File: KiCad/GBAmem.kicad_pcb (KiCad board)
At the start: 4 copper layers, 18.2 x 18.3 mm, 2 parts, among them IC1 IS62WV12816EBLL-45TLI, U1 HY62LF16206A-LT12C

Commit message: Add build files and initial code
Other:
- board text added: "github.com/HorstBaerbel/GBA-mem v1.0"
- board text removed: "github.com/HorstBaerbel/GBAmem v1.0"
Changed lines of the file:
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@@
       (effects (font (size 1.27 1.27) (thickness 0.254)))
     )
+    (fp_line (start -6.625 -9.52) (end 6.625 -9.52) (layer F.CrtYd) (width 0.05))
+    (fp_line (start 6.625 -9.52) (end 6.625 9.52) (layer F.CrtYd) (width 0.05))
+    (fp_line (start 6.625 9.52) (end -6.625 9.52) (layer F.CrtYd) (width 0.05))
+    (fp_line (start -6.625 9.52) (end -6.625 -9.52) (layer F.CrtYd) (width 0.05))
+    (fp_line (start -5.08 -9.205) (end 5.08 -9.205) (layer F.Fab) (width 0.1))
+    (fp_line (start 5.08 -9.205) (end 5.08 9.205) (layer F.Fab) (width 0.1))
+    (fp_line (start 5.08 9.205) (end -5.08 9.205) (layer F.Fab) (width 0.1))
+    (fp_line (start -5.08 9.205) (end -5.08 -9.205) (layer F.Fab) (width 0.1))
+    (fp_line (start -5.08 -8.405) (end -4.28 -9.205) (layer F.Fab) (width 0.1))
+    (fp_line (start -4.73 -9.205) (end 4.73 -9.205) (layer F.SilkS) (width 0.2))
+    (fp_line (start 4.73 -9.205) (end 4.73 9.205) (layer F.SilkS) (width 0.2))
+    (fp_line (start 4.73 9.205) (end -4.73 9.205) (layer F.SilkS) (width 0.2))
+    (fp_line (start -4.73 9.205) (end -4.73 -9.205) (layer F.SilkS) (width 0.2))
     (fp_line (start -6.375 -9.05) (end -5.08 -9.05) (layer F.SilkS) (width 0.2))
-    (fp_line (start -4.73 9.205) (end -4.73 -9.205) (layer F.SilkS) (width 0.2))
-    (fp_line (start 4.73 9.205) (end -4.73 9.205) (layer F.SilkS) (width 0.2))
-    (fp_line (start 4.73 -9.205) (end 4.73 9.205) (layer F.SilkS) (width 0.2))
-    (fp_line (start -4.73 -9.205) (end 4.73 -9.205) (layer F.SilkS) (width 0.2))
-    (fp_line (start -5.08 -8.405) (end -4.28 -9.205) (layer F.Fab) (width 0.1))
-    (fp_line (start -5.08 9.205) (end -5.08 -9.205) (layer F.Fab) (width 0.1))
-    (fp_line (start 5.08 9.205) (end -5.08 9.205) (layer F.Fab) (width 0.1))
-    (fp_line (start 5.08 -9.205) (end 5.08 9.205) (layer F.Fab) (width 0.1))
-    (fp_line (start -5.08 -9.205) (end 5.08 -9.205) (layer F.Fab) (width 0.1))
-    (fp_line (start -6.625 9.52) (end -6.625 -9.52) (layer F.CrtYd) (width 0.05))
-    (fp_line (start 6.625 9.52) (end -6.625 9.52) (layer F.CrtYd) (width 0.05))
-    (fp_line (start 6.625 -9.52) (end 6.625 9.52) (layer F.CrtYd) (width 0.05))
-    (fp_line (start -6.625 -9.52) (end 6.625 -9.52) (layer F.CrtYd) (width 0.05))
     (fp_text user %R (at 0 0) (layer F.Fab) hide
       (effects (font (size 1.27 1.27) (thickness 0.254)))
@@
       (effects (font (size 0.8 0.8) (thickness 0.125)) (justify mirror))
     )
+    (fp_line (start 9.6 6.3) (end 9.6 -6.3) (layer B.CrtYd) (width 0.12))
+    (fp_line (start 9.6 -6.3) (end -9.2 -6.3) (layer B.CrtYd) (width 0.12))
+    (fp_line (start -9.2 -6.3) (end -9.2 6.3) (layer B.CrtYd) (width 0.12))
+    (fp_line (start -9.2 6.3) (end 9.6 6.3) (layer B.CrtYd) (width 0.12))
+    (fp_line (start 8.4 -6.1) (end 8.4 6.1) (layer B.Fab) (width 0.12))
+    (fp_line (start 8.4 6.1) (end -8 6.1) (layer B.Fab) (width 0.12))
+    (fp_line (start -8 6.1) (end -8 -6.1) (layer B.Fab) (width 0.12))
     (fp_line (start -8 -6.1) (end 8.4 -6.1) (layer B.Fab) (width 0.12))
-    (fp_line (start -8 6.1) (end -8 -6.1) (layer B.Fab) (width 0.12))
-    (fp_line (start 8.4 6.1) (end -8 6.1) (layer B.Fab) (width 0.12))
-    (fp_line (start 8.4 -6.1) (end 8.4 6.1) (layer B.Fab) (width 0.12))
-    (fp_line (start -9.2 6.3) (end 9.6 6.3) (layer B.CrtYd) (width 0.12))
-    (fp_line (start -9.2 -6.3) (end -9.2 6.3) (layer B.CrtYd) (width 0.12))
-    (fp_line (start 9.6 -6.3) (end -9.2 -6.3) (layer B.CrtYd) (width 0.12))
-    (fp_line (start 9.6 6.3) (end 9.6 -6.3) (layer B.CrtYd) (width 0.12))
     (fp_text user "Flipped / Breakout" (at 0 5.3) (layer B.CrtYd)
       (effects (font (size 0.7 0.7) (thickness 0.125)) (justify mirror))
@@
     (effects (font (size 0.8 0.8) (thickness 0.2)))
   )
-  (gr_text "github.com/HorstBaerbel/GBAmem v1.0" (at 171.0055 89.789 90) (layer F.SilkS)
-    (effects (font (size 0.58 0.58) (thickness 0.125)))
+  (gr_text "github.com/HorstBaerbel/GBA-mem v1.0" (at 171.0055 89.789 90) (layer F.SilkS)
+    (effects (font (size 0.56 0.56) (thickness 0.125)))
   )
   (segment (start 169.3758 93.293) (end 169.3758 92.36) (width 0.1) (layer Front) (net 1))

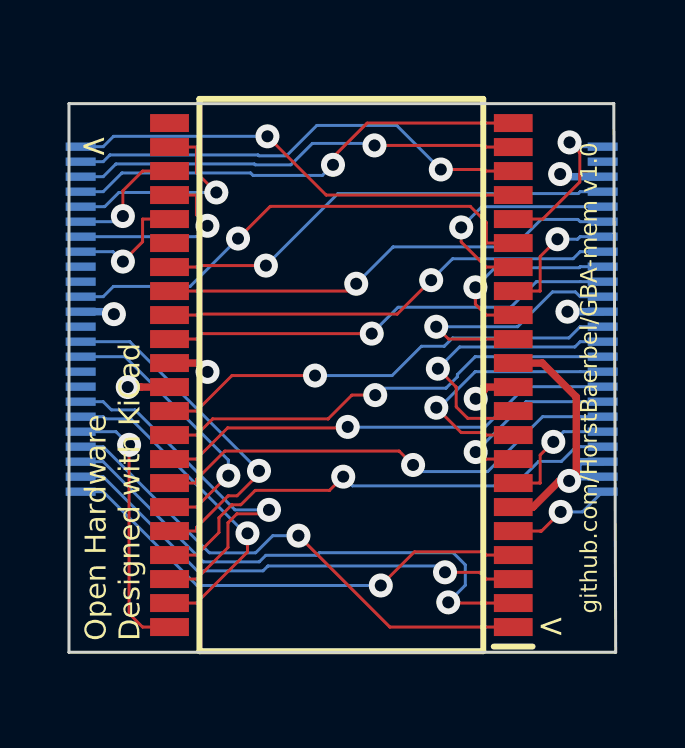
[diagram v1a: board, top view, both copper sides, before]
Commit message: Update PCB with positioning markers
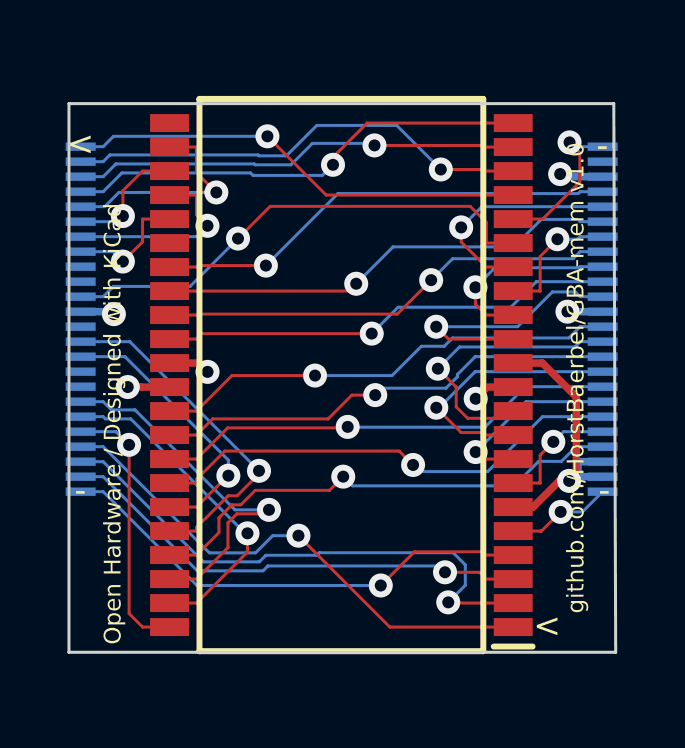
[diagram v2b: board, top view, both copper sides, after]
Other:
- board text added: "-"
- board text added: "Open Hardware / Designed with KiCad"
- board text removed: "Open Hardware Designed with KiCad"
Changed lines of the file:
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@@
   (general
     (thickness 1.6)
-    (drawings 8)
+    (drawings 11)
     (tracks 365)
     (zones 0)
@@
       (effects (font (size 1.27 1.27) (thickness 0.254)))
     )
+    (fp_line (start -6.375 -9.05) (end -5.08 -9.05) (layer F.SilkS) (width 0.2))
+    (fp_line (start -4.73 9.205) (end -4.73 -9.205) (layer F.SilkS) (width 0.2))
+    (fp_line (start 4.73 9.205) (end -4.73 9.205) (layer F.SilkS) (width 0.2))
+    (fp_line (start 4.73 -9.205) (end 4.73 9.205) (layer F.SilkS) (width 0.2))
+    (fp_line (start -4.73 -9.205) (end 4.73 -9.205) (layer F.SilkS) (width 0.2))
+    (fp_line (start -5.08 -8.405) (end -4.28 -9.205) (layer F.Fab) (width 0.1))
+    (fp_line (start -5.08 9.205) (end -5.08 -9.205) (layer F.Fab) (width 0.1))
+    (fp_line (start 5.08 9.205) (end -5.08 9.205) (layer F.Fab) (width 0.1))
+    (fp_line (start 5.08 -9.205) (end 5.08 9.205) (layer F.Fab) (width 0.1))
+    (fp_line (start -5.08 -9.205) (end 5.08 -9.205) (layer F.Fab) (width 0.1))
+    (fp_line (start -6.625 9.52) (end -6.625 -9.52) (layer F.CrtYd) (width 0.05))
+    (fp_line (start 6.625 9.52) (end -6.625 9.52) (layer F.CrtYd) (width 0.05))
+    (fp_line (start 6.625 -9.52) (end 6.625 9.52) (layer F.CrtYd) (width 0.05))
     (fp_line (start -6.625 -9.52) (end 6.625 -9.52) (layer F.CrtYd) (width 0.05))
-    (fp_line (start 6.625 -9.52) (end 6.625 9.52) (layer F.CrtYd) (width 0.05))
-    (fp_line (start 6.625 9.52) (end -6.625 9.52) (layer F.CrtYd) (width 0.05))
-    (fp_line (start -6.625 9.52) (end -6.625 -9.52) (layer F.CrtYd) (width 0.05))
-    (fp_line (start -5.08 -9.205) (end 5.08 -9.205) (layer F.Fab) (width 0.1))
-    (fp_line (start 5.08 -9.205) (end 5.08 9.205) (layer F.Fab) (width 0.1))
-    (fp_line (start 5.08 9.205) (end -5.08 9.205) (layer F.Fab) (width 0.1))
-    (fp_line (start -5.08 9.205) (end -5.08 -9.205) (layer F.Fab) (width 0.1))
-    (fp_line (start -5.08 -8.405) (end -4.28 -9.205) (layer F.Fab) (width 0.1))
-    (fp_line (start -4.73 -9.205) (end 4.73 -9.205) (layer F.SilkS) (width 0.2))
-    (fp_line (start 4.73 -9.205) (end 4.73 9.205) (layer F.SilkS) (width 0.2))
-    (fp_line (start 4.73 9.205) (end -4.73 9.205) (layer F.SilkS) (width 0.2))
-    (fp_line (start -4.73 9.205) (end -4.73 -9.205) (layer F.SilkS) (width 0.2))
-    (fp_line (start -6.375 -9.05) (end -5.08 -9.05) (layer F.SilkS) (width 0.2))
     (fp_text user %R (at 0 0) (layer F.Fab) hide
       (effects (font (size 1.27 1.27) (thickness 0.254)))
@@
       (effects (font (size 0.8 0.8) (thickness 0.125)) (justify mirror))
     )
+    (fp_line (start -8 -6.1) (end 8.4 -6.1) (layer B.Fab) (width 0.12))
+    (fp_line (start -8 6.1) (end -8 -6.1) (layer B.Fab) (width 0.12))
+    (fp_line (start 8.4 6.1) (end -8 6.1) (layer B.Fab) (width 0.12))
+    (fp_line (start 8.4 -6.1) (end 8.4 6.1) (layer B.Fab) (width 0.12))
+    (fp_line (start -9.2 6.3) (end 9.6 6.3) (layer B.CrtYd) (width 0.12))
+    (fp_line (start -9.2 -6.3) (end -9.2 6.3) (layer B.CrtYd) (width 0.12))
+    (fp_line (start 9.6 -6.3) (end -9.2 -6.3) (layer B.CrtYd) (width 0.12))
     (fp_line (start 9.6 6.3) (end 9.6 -6.3) (layer B.CrtYd) (width 0.12))
-    (fp_line (start 9.6 -6.3) (end -9.2 -6.3) (layer B.CrtYd) (width 0.12))
-    (fp_line (start -9.2 -6.3) (end -9.2 6.3) (layer B.CrtYd) (width 0.12))
-    (fp_line (start -9.2 6.3) (end 9.6 6.3) (layer B.CrtYd) (width 0.12))
-    (fp_line (start 8.4 -6.1) (end 8.4 6.1) (layer B.Fab) (width 0.12))
-    (fp_line (start 8.4 6.1) (end -8 6.1) (layer B.Fab) (width 0.12))
-    (fp_line (start -8 6.1) (end -8 -6.1) (layer B.Fab) (width 0.12))
-    (fp_line (start -8 -6.1) (end 8.4 -6.1) (layer B.Fab) (width 0.12))
     (fp_text user "Flipped / Breakout" (at 0 5.3) (layer B.CrtYd)
       (effects (font (size 0.7 0.7) (thickness 0.125)) (justify mirror))
@@
       (net 40 /A15))
   )
+  (gr_text - (at 154.051 93.5355) (layer F.SilkS)
+    (effects (font (size 0.8 0.8) (thickness 0.2)))
+  )
+  (gr_text - (at 171.5135 93.5355) (layer F.SilkS)
+    (effects (font (size 0.8 0.8) (thickness 0.2)))
+  )
+  (gr_text - (at 171.45 82.042) (layer F.SilkS)
+    (effects (font (size 0.8 0.8) (thickness 0.2)))
+  )
   (gr_line (start 171.8945 98.933) (end 153.67 98.933) (layer Edge.Cuts) (width 0.1))
   (gr_line (start 153.67 98.933) (end 153.67 80.645) (layer Edge.Cuts) (width 0.1))
   (gr_line (start 153.67 80.645) (end 171.831 80.645) (layer Edge.Cuts) (width 0.1))
   (gr_line (start 171.831 80.645) (end 171.8945 98.933) (layer Edge.Cuts) (width 0.1))
-  (gr_text "Open Hardware\nDesigned with KiCad" (at 155.1305 98.552 90) (layer F.SilkS)
-    (effects (font (size 0.7 0.7) (thickness 0.15)) (justify left))
-  )
-  (gr_text < (at 154.4955 82.042) (layer F.SilkS)
+  (gr_text "Open Hardware / Designed with KiCad" (at 155.1305 98.679 90) (layer F.SilkS)
+    (effects (font (size 0.56 0.56) (thickness 0.125)) (justify left))
+  )
+  (gr_text < (at 154.051 81.9785) (layer F.SilkS)
     (effects (font (size 0.8 0.8) (thickness 0.2)))
   )
-  (gr_text < (at 169.7355 98.044) (layer F.SilkS)
+  (gr_text < (at 169.6085 98.044) (layer F.SilkS)
     (effects (font (size 0.8 0.8) (thickness 0.2)))
   )
-  (gr_text "github.com/HorstBaerbel/GBA-mem v1.0" (at 171.0055 89.789 90) (layer F.SilkS)
+  (gr_text "github.com/HorstBaerbel/GBA-mem v1.0" (at 170.561 89.789 90) (layer F.SilkS)
     (effects (font (size 0.56 0.56) (thickness 0.125)))
   )
